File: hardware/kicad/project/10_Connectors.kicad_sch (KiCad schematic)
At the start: 0 parts

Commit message: feat(hardware): TB-HW-002 — populate all 12 schematic sheets with components
Populated 235 component symbols across all 12 KiCad schematic sheets:
- 01_Power: Reverse polarity, TVS (SMCJ33A), buck (LMR33630), LDO (TPS7A1633), VREF (REF5050) — 30 symbols
- 02_MCU: S32K344 (6 units), clock (40MHz+32kHz), decoupling, reset, boot config, LEDs — 30 symbols
- 03_CAN: 4x TJA1043 with CM chokes (ACT45B-510), split termination, bus filter caps — 36 symbols
- 04_USB: Molex USB-C, TPD2EUSB30 ESD, CC resistors, eFuse, Ethernet PHY footprint — 9 symbols
- 05_Inputs: 8 analog channels (RC+clamp), 2x CJ125 WBO2, 2x TLE2072 knock amps — 50 symbols
- 06_Injectors: TLE8888-2QK (8-ch P&H), flyback diodes, current sense — 14 symbols
- 07_Ignition: 6x ISL9V3040S3 IGBTs with gate resistors (100R), pull-downs (10k) — 24 symbols
- 08_Outputs: DRV8873 ETC H-bridge, TLE8110ED low-side (boost+relays), BTS4140N tach — 12 symbols
- 09_Protection: TPS3850G33 watchdog, safe-state FET, ESD diodes (PESD5V0) — 14 symbols
- 10_Connectors: 42-pin Deutsch DTM (2 units), 2x CAN 4-pin, diagnostic 4-pin — 5 symbols
- 11_Programming: TC2050 SWD, 8 test points, production security notes — 11 symbols
- 00_Cover: Block diagram, BOM summary, spec references, revision history

Symbol library: 18 custom symbols with complete pin assignments
Components from COMPONENT_SELECTION.md r0.1
42-pin connector per INTERFACE_SPECIFICATION.md (authority)
All MCU pins per MCU_SELECTION.md pin allocation
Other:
- note added: "42-Pin Deutsch DTM | CAN x2 (4-pin Deutsch) | Diag (4-pin Deutsch) | USB-C | SWD | Expansion"
- note added: "Bank A (1-21): Power, Injectors, Ignition | Bank B (22-42): ETC, Sensors, WBO2, Knock, Boost, Relays"
- note added: "CAN CONNECTORS (2x 4-Pin Deutsch DTM)"
- note added: "CAN0: Pin1=GND, Pin2=CAN_H, Pin3=CAN_L, Pin4=VBAT(fused)"
- note added: "CAN1: Pin1=GND, Pin2=CAN_H, Pin3=CAN_L, Pin4=VBAT(fused)"
- note added: "CAN2 diagnostic port: Pin1=GND, Pin2=CAN2_H, Pin3=CAN2_L, Pin4=VBAT(1A fused)"
- note added: "DIAGNOSTIC CONNECTOR (4-Pin Deutsch DTM)"
- note added: "MAIN HARNESS CONNECTOR"
- note added: "Mating: DTM04-12PB plug | Gold-plated sockets | 14-22 AWG per pin function"
- note added: "Pin Summary: Main 42-pin (35 used, 7 spare) | CAN x2 (8 used) | Diag (4 used) | USB-C (4 used) | DEBUG (5 used)"
- note added: "Ref: docs/hardware/INTERFACE_SPECIFICATION.md §1-6 | TE Connectivity Deutsch DTM series"
- note added: "USB-C: Molex 105450-0101 — see Sheet 04_USB"
- note removed: "34-pin AMPSEAL 16 main harness | CAN1, CAN2 DEUTSCH DT 4-pin"
- note removed: "Ref: docs/hardware/INTERFACE_SPECIFICATION.md — 34-pin frozen pinout"
- note removed: "USB-C (panel mount) | SWD debug (Tag-Connect) | Expansion header"
- title: 7100CPT ECU — 34-Pin, CAN, USB, Debug, Exp -> 7100CPT ECU — 42-Pin DTM, CAN, USB, SWD, Expansion
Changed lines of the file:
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@@
-(kicad_sch (version 20240108) (generator "eeschema")
+(kicad_sch (version 20240108) (generator "7100CPT-schematic-gen")
   (paper "A3")
   (title_block
-    (title "7100CPT ECU — 34-Pin, CAN, USB, Debug, Exp")
+    (title "7100CPT ECU — 42-Pin DTM, CAN, USB, SWD, Expansion")
     (date "2026-07-03")
-    (rev "0.1")
+    (rev "0.2")
     (company "${COMPANY}")
-    (comment 1 "34-pin AMPSEAL 16 main, CAN x2, USB-C, SWD, expansion header")
+    (comment 1 "Main harness (42-pin DTM), CAN x2, diagnostic port, USB-C, debug")
     (comment 2 "NXP S32K344 | rusEFI Firmware | IPC Class 3")
     (comment 3 "High-Tg FR-4 (TG170+) | ENIG | 1.6 mm")
-    (comment 4 "REUSE_MATRIX.md — NXP Reference Following")
+    (comment 4 "Phase 0 Approved | REUSE_MATRIX gate passed")
     (comment 5 "-40C to +85C | IP67 Target | 6-Layer")
   )
-  (symbol_instances)
-  (text "CONNECTORS — Sheet 10"
-    (at 25 24 0) (effects (font (size 3.0 3.0) bold) (justify left bottom)))
-  (text "34-pin AMPSEAL 16 main harness | CAN1, CAN2 DEUTSCH DT 4-pin"
-    (at 25 30 0) (effects (font (size 1.5 1.5)) (justify left bottom)))
-  (text "USB-C (panel mount) | SWD debug (Tag-Connect) | Expansion header"
-    (at 25 36 0) (effects (font (size 1.5 1.5)) (justify left bottom)))
-  (text "Ref: docs/hardware/INTERFACE_SPECIFICATION.md — 34-pin frozen pinout"
-    (at 25 42 0) (effects (font (size 1.27 1.27)) (justify left bottom)))
+  (symbol_instances
+  (symbol (lib_id "7100CPT:DTM_42PIN") (at 100 200 0) (unit 1)
+    (exclude_from_sim yes) (in_bom yes) (on_board yes) (dnp no)
+    (property "Reference" "J1A" (at 100 200 0) (effects (font (size 1.27 1.27))))
+    (property "Value" "DTM06-12SA_Bank_A" (at 100 193.65 0) (effects (font (size 1.27 1.27))))
+  )
+  (symbol (lib_id "7100CPT:DTM_42PIN") (at 100 120 0) (unit 2)
+    (exclude_from_sim yes) (in_bom yes) (on_board yes) (dnp no)
+    (property "Reference" "J1B" (at 100 120 0) (effects (font (size 1.27 1.27))))
+    (property "Value" "DTM06-12SA_Bank_B" (at 100 113.65 0) (effects (font (size 1.27 1.27))))
+  )
+  (symbol (lib_id "Connector:Conn_01x04_Male") (at 50 70 0) (unit 1)
+    (exclude_from_sim yes) (in_bom yes) (on_board yes) (dnp no)
+    (property "Reference" "J3" (at 50 70 0) (effects (font (size 1.27 1.27))))
+    (property "Value" "DTM06-4S_CAN0" (at 50 63.65 0) (effects (font (size 1.27 1.27))))
+  )
+  (symbol (lib_id "Connector:Conn_01x04_Male") (at 250 70 0) (unit 1)
+    (exclude_from_sim yes) (in_bom yes) (on_board yes) (dnp no)
+    (property "Reference" "J4" (at 250 70 0) (effects (font (size 1.27 1.27))))
+    (property "Value" "DTM06-4S_CAN1" (at 250 63.65 0) (effects (font (size 1.27 1.27))))
+  )
+  (symbol (lib_id "Connector:Conn_01x04_Male") (at 50 30 0) (unit 1)
+    (exclude_from_sim yes) (in_bom yes) (on_board yes) (dnp no)
+    (property "Reference" "J5" (at 50 30 0) (effects (font (size 1.27 1.27))))
+    (property "Value" "DTM06-4S_DIAG" (at 50 23.65 0) (effects (font (size 1.27 1.27))))
+  )
+  )
+  (text "CONNECTORS — Sheet 10" (at 25 260 0) (effects (font (size 3.0 3.0) bold) (justify left bottom)))
+  (text "42-Pin Deutsch DTM | CAN x2 (4-pin Deutsch) | Diag (4-pin Deutsch) | USB-C | SWD | Expansion" (at 25 254 0) (effects (font (size 1.5 1.5)) (justify left bottom)))
+  (text "MAIN HARNESS CONNECTOR" (at 25 230 0) (effects (font (size 1.5 1.5) bold) (justify left bottom)))
+  (text "Bank A (1-21): Power, Injectors, Ignition | Bank B (22-42): ETC, Sensors, WBO2, Knock, Boost, Relays" (at 100 100 0) (effects (font (size 1.27 1.27)) (justify left bottom)))
+  (text "Mating: DTM04-12PB plug | Gold-plated sockets | 14-22 AWG per pin function" (at 100 93 0) (effects (font (size 1.27 1.27)) (justify left bottom)))
+  (text "CAN CONNECTORS (2x 4-Pin Deutsch DTM)" (at 25 90 0) (effects (font (size 1.5 1.5) bold) (justify left bottom)))
+  (text "CAN0: Pin1=GND, Pin2=CAN_H, Pin3=CAN_L, Pin4=VBAT(fused)" (at 50 55 0) (effects (font (size 1.0 1.0)) (justify left bottom)))
+  (text "CAN1: Pin1=GND, Pin2=CAN_H, Pin3=CAN_L, Pin4=VBAT(fused)" (at 250 55 0) (effects (font (size 1.0 1.0)) (justify left bottom)))
+  (text "DIAGNOSTIC CONNECTOR (4-Pin Deutsch DTM)" (at 25 50 0) (effects (font (size 1.5 1.5) bold) (justify left bottom)))
+  (text "CAN2 diagnostic port: Pin1=GND, Pin2=CAN2_H, Pin3=CAN2_L, Pin4=VBAT(1A fused)" (at 50 15 0) (effects (font (size 1.0 1.0)) (justify left bottom)))
+  (text "USB-C: Molex 105450-0101 — see Sheet 04_USB" (at 400 50 0) (effects (font (size 1.27 1.27)) (justify left bottom)))
+  (text "Pin Summary: Main 42-pin (35 used, 7 spare) | CAN x2 (8 used) | Diag (4 used) | USB-C (4 used) | DEBUG (5 used)" (at 25 -10 0) (effects (font (size 1.27 1.27)) (justify left bottom)))
+  (text "Ref: docs/hardware/INTERFACE_SPECIFICATION.md §1-6 | TE Connectivity Deutsch DTM series" (at 25 -17 0) (effects (font (size 1.27 1.27)) (justify left bottom)))
   (sheet_instances
     (path "/10_connectors/" (page "11"))

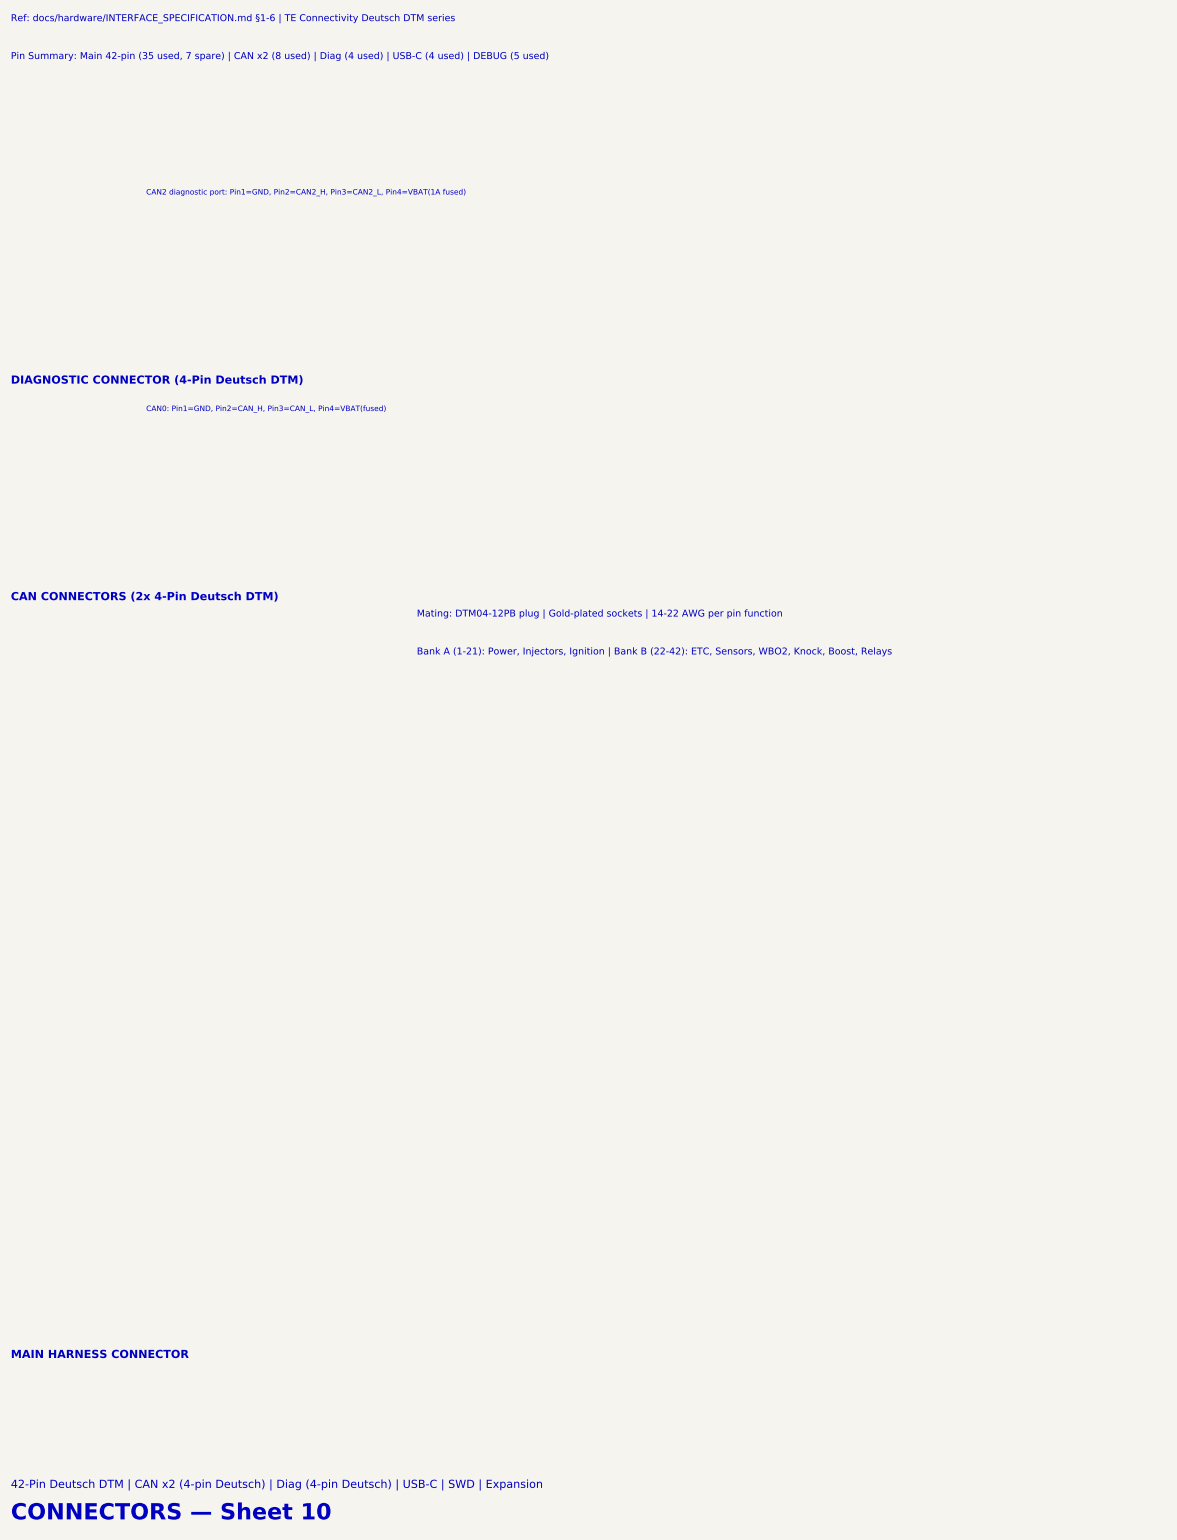
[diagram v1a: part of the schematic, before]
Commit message: fix(hardware): reconcile connector spec to 34-pin AMPSEAL, wire TP5-GND on sheet 11, add DESIGN_NOTES for known gaps
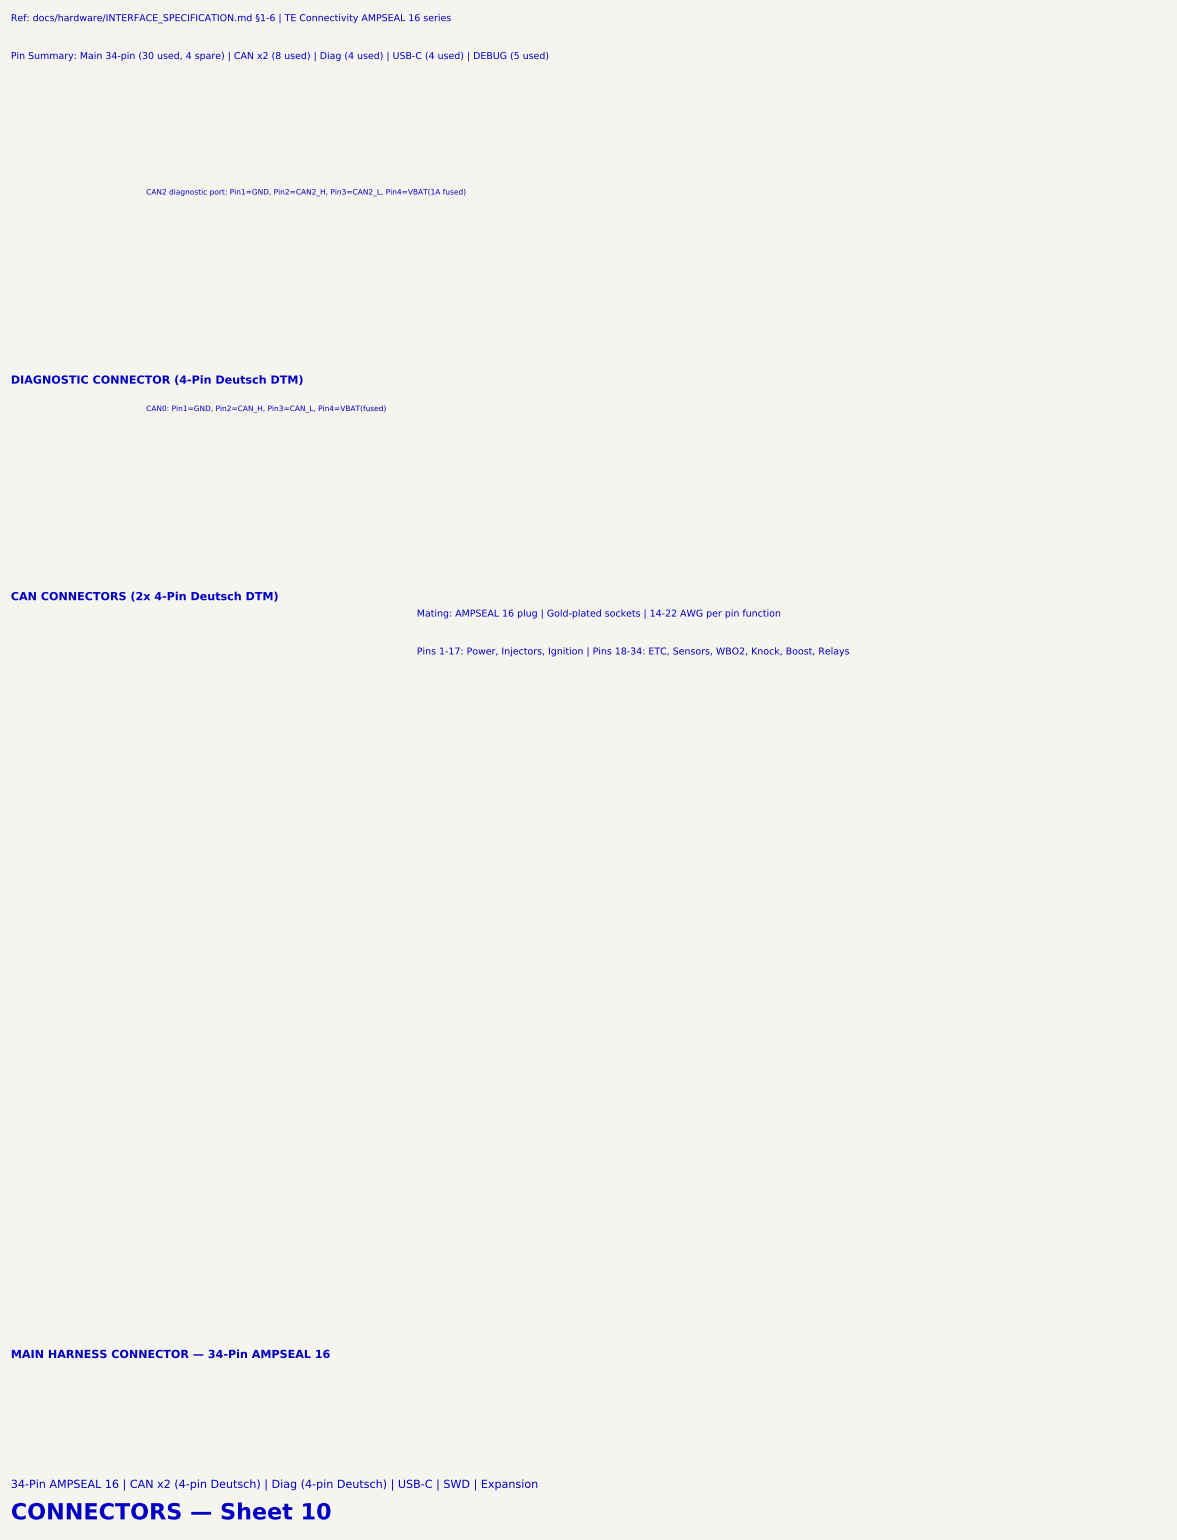
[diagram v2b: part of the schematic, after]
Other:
- note added: "34-Pin AMPSEAL 16 | CAN x2 (4-pin Deutsch) | Diag (4-pin Deutsch) | USB-C | SWD | Expansion"
- note added: "MAIN HARNESS CONNECTOR — 34-Pin AMPSEAL 16"
- note added: "Mating: AMPSEAL 16 plug | Gold-plated sockets | 14-22 AWG per pin function"
- note added: "Pin Summary: Main 34-pin (30 used, 4 spare) | CAN x2 (8 used) | Diag (4 used) | USB-C (4 used) | DEBUG (5 used)"
- note added: "Pins 1-17: Power, Injectors, Ignition | Pins 18-34: ETC, Sensors, WBO2, Knock, Boost, Relays"
- note added: "Ref: docs/hardware/INTERFACE_SPECIFICATION.md §1-6 | TE Connectivity AMPSEAL 16 series"
- note removed: "42-Pin Deutsch DTM | CAN x2 (4-pin Deutsch) | Diag (4-pin Deutsch) | USB-C | SWD | Expansion"
- note removed: "Bank A (1-21): Power, Injectors, Ignition | Bank B (22-42): ETC, Sensors, WBO2, Knock, Boost, Relays"
- note removed: "MAIN HARNESS CONNECTOR"
- note removed: "Mating: DTM04-12PB plug | Gold-plated sockets | 14-22 AWG per pin function"
- note removed: "Pin Summary: Main 42-pin (35 used, 7 spare) | CAN x2 (8 used) | Diag (4 used) | USB-C (4 used) | DEBUG (5 used)"
- note removed: "Ref: docs/hardware/INTERFACE_SPECIFICATION.md §1-6 | TE Connectivity Deutsch DTM series"
- title: 7100CPT ECU — 42-Pin DTM, CAN, USB, SWD, Expansion -> 7100CPT ECU — 34-Pin AMPSEAL, CAN, USB, SWD, Expansion
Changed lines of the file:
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@@
   (paper "A3")
   (title_block
-    (title "7100CPT ECU — 42-Pin DTM, CAN, USB, SWD, Expansion")
+    (title "7100CPT ECU — 34-Pin AMPSEAL, CAN, USB, SWD, Expansion")
     (date "2026-07-03")
     (rev "0.2")
     (company "${COMPANY}")
-    (comment 1 "Main harness (42-pin DTM), CAN x2, diagnostic port, USB-C, debug")
+    (comment 1 "Main harness (34-pin AMPSEAL 16), CAN x2, diagnostic port, USB-C, debug")
     (comment 2 "NXP S32K344 | rusEFI Firmware | IPC Class 3")
     (comment 3 "High-Tg FR-4 (TG170+) | ENIG | 1.6 mm")
@@
   )
   (text "CONNECTORS — Sheet 10" (at 25 260 0) (effects (font (size 3.0 3.0) bold) (justify left bottom)))
-  (text "42-Pin Deutsch DTM | CAN x2 (4-pin Deutsch) | Diag (4-pin Deutsch) | USB-C | SWD | Expansion" (at 25 254 0) (effects (font (size 1.5 1.5)) (justify left bottom)))
-  (text "MAIN HARNESS CONNECTOR" (at 25 230 0) (effects (font (size 1.5 1.5) bold) (justify left bottom)))
-  (text "Bank A (1-21): Power, Injectors, Ignition | Bank B (22-42): ETC, Sensors, WBO2, Knock, Boost, Relays" (at 100 100 0) (effects (font (size 1.27 1.27)) (justify left bottom)))
-  (text "Mating: DTM04-12PB plug | Gold-plated sockets | 14-22 AWG per pin function" (at 100 93 0) (effects (font (size 1.27 1.27)) (justify left bottom)))
+  (text "34-Pin AMPSEAL 16 | CAN x2 (4-pin Deutsch) | Diag (4-pin Deutsch) | USB-C | SWD | Expansion" (at 25 254 0) (effects (font (size 1.5 1.5)) (justify left bottom)))
+  (text "MAIN HARNESS CONNECTOR — 34-Pin AMPSEAL 16" (at 25 230 0) (effects (font (size 1.5 1.5) bold) (justify left bottom)))
+  (text "Pins 1-17: Power, Injectors, Ignition | Pins 18-34: ETC, Sensors, WBO2, Knock, Boost, Relays" (at 100 100 0) (effects (font (size 1.27 1.27)) (justify left bottom)))
+  (text "Mating: AMPSEAL 16 plug | Gold-plated sockets | 14-22 AWG per pin function" (at 100 93 0) (effects (font (size 1.27 1.27)) (justify left bottom)))
   (text "CAN CONNECTORS (2x 4-Pin Deutsch DTM)" (at 25 90 0) (effects (font (size 1.5 1.5) bold) (justify left bottom)))
   (text "CAN0: Pin1=GND, Pin2=CAN_H, Pin3=CAN_L, Pin4=VBAT(fused)" (at 50 55 0) (effects (font (size 1.0 1.0)) (justify left bottom)))
@@
   (text "CAN2 diagnostic port: Pin1=GND, Pin2=CAN2_H, Pin3=CAN2_L, Pin4=VBAT(1A fused)" (at 50 15 0) (effects (font (size 1.0 1.0)) (justify left bottom)))
   (text "USB-C: Molex 105450-0101 — see Sheet 04_USB" (at 400 50 0) (effects (font (size 1.27 1.27)) (justify left bottom)))
-  (text "Pin Summary: Main 42-pin (35 used, 7 spare) | CAN x2 (8 used) | Diag (4 used) | USB-C (4 used) | DEBUG (5 used)" (at 25 -10 0) (effects (font (size 1.27 1.27)) (justify left bottom)))
-  (text "Ref: docs/hardware/INTERFACE_SPECIFICATION.md §1-6 | TE Connectivity Deutsch DTM series" (at 25 -17 0) (effects (font (size 1.27 1.27)) (justify left bottom)))
+  (text "Pin Summary: Main 34-pin (30 used, 4 spare) | CAN x2 (8 used) | Diag (4 used) | USB-C (4 used) | DEBUG (5 used)" (at 25 -10 0) (effects (font (size 1.27 1.27)) (justify left bottom)))
+  (text "Ref: docs/hardware/INTERFACE_SPECIFICATION.md §1-6 | TE Connectivity AMPSEAL 16 series" (at 25 -17 0) (effects (font (size 1.27 1.27)) (justify left bottom)))
   (sheet_instances
     (path "/10_connectors/" (page "11"))
